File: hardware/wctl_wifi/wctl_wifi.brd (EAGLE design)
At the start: 40.4 x 26.8 mm, 9 parts, among them U1 Value

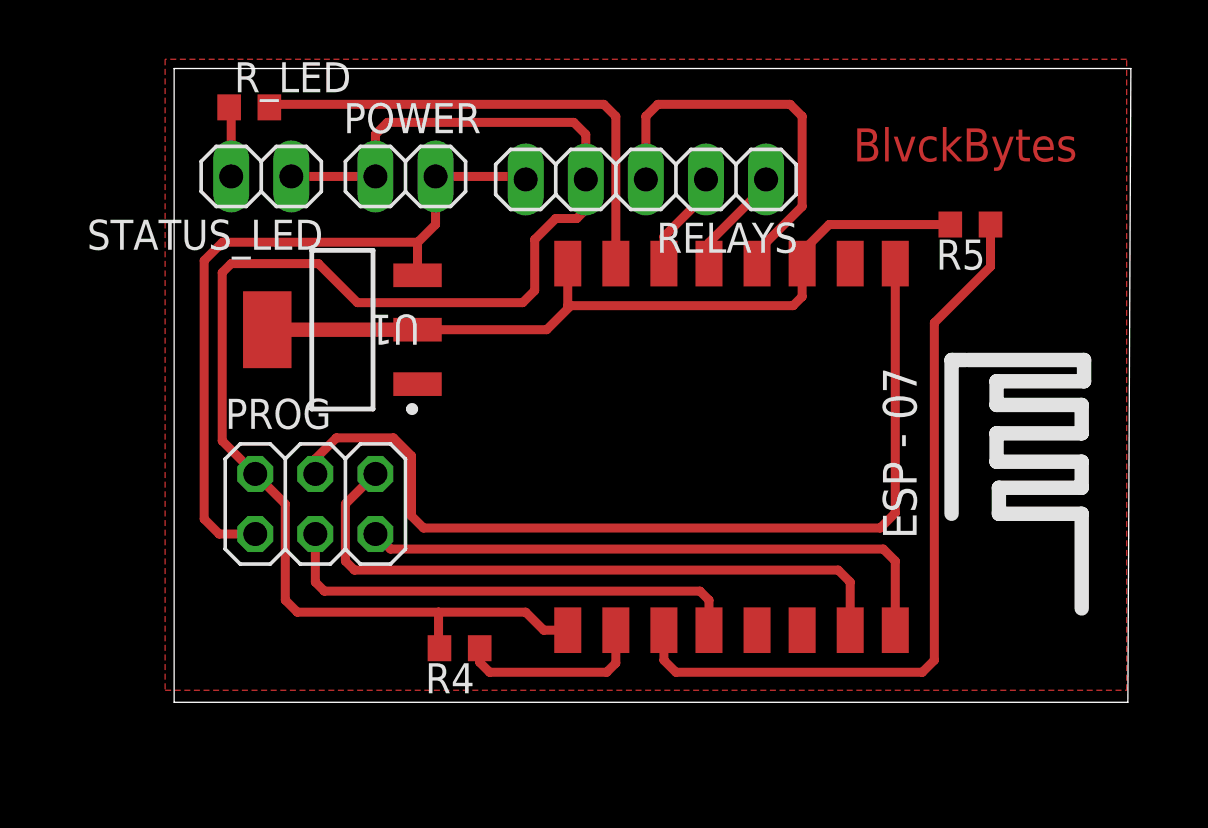
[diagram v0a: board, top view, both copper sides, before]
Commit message: Migrated back to ESP32, updated pins in code and updated hardware, also updated readme
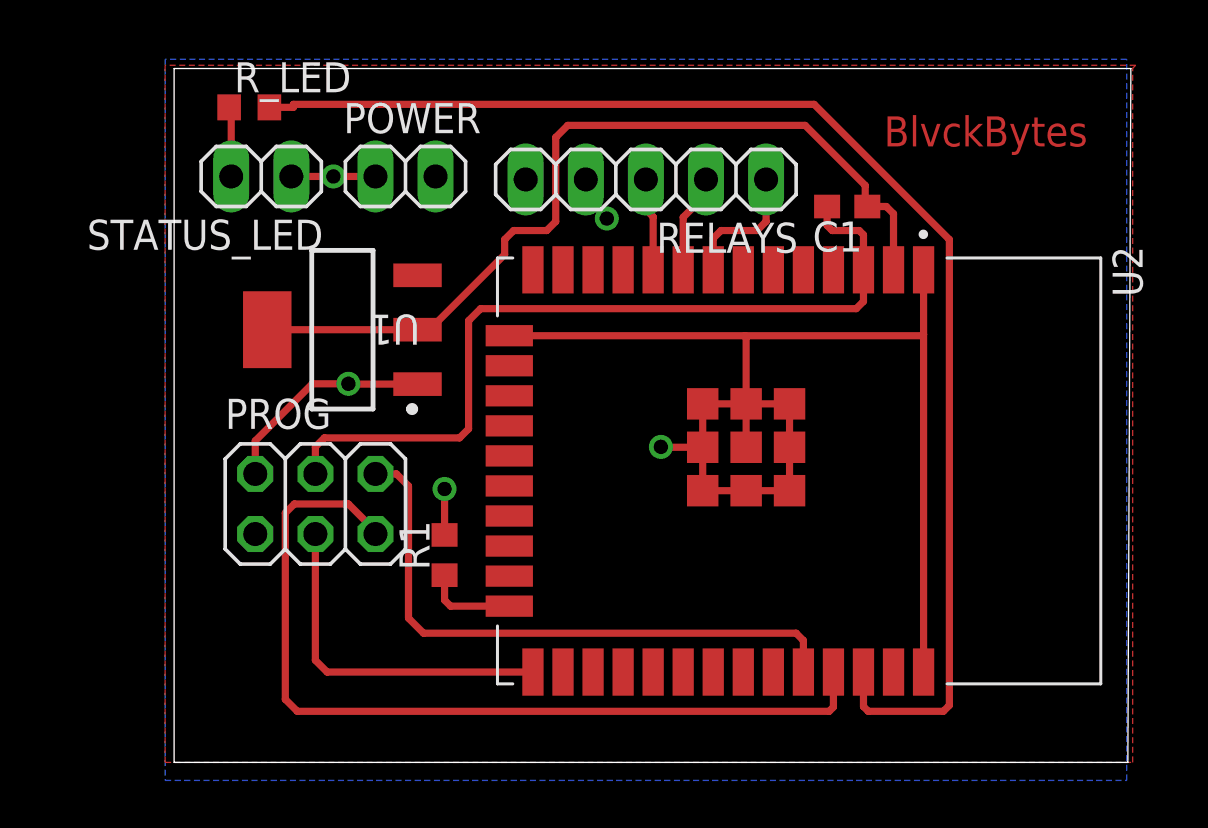
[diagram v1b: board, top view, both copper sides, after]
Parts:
- removed R4, R5: 10k, rcl:R0603
- removed U$2: ESP07, esp-07:ESP07
- added C1: (no value), rcl:C0603
- added R1: 10k, rcl:R0603
- added U2: ESP32-WROOM-32D, ESP32-WROOM-32D:MODULE_ESP32-WROOM-32D
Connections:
- removed net N$4: R_LED.2, U$2.GPIO13
- removed net N$6: R5.1, U$2.GPIO2
- removed net N$7: R4.1, U$2.GPIO15
- new net N$2: R_LED.2, U2.36
- new net N$3: R1.1, U2.24
- net +3V3: now also C1.1, U2.2; no longer R5.2, U$2.CH_PD, U$2.VCC
- net GND: now also R1.2, U2.1, U2.15, U2.38, U2.39_1, U2.39_2, U2.39_3, U2.39_4, U2.39_5, U2.39_6, U2.39_7, U2.39_8, U2.39_9; no longer R4.2, U$2.GND
- net PROG: now also U2.25; no longer U$2.GPIO0
- net RELAYS_DATA: now also U2.10; no longer U$2.GPIO16
- net RELAYS_SHIFT: now also U2.8; no longer U$2.GPIO14
- net RELAYS_STORE: now also U2.9; no longer U$2.GPIO12
- net RESET: now also C1.2, U2.3; no longer U$2.RESET
- net RX: now also U2.34; no longer U$2.RX
- net TX: now also U2.35; no longer U$2.TX
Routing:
- net N$2: track 0.00 -> 56.2 mm
- net N$6: track 32.5 -> 0.00 mm
- net +5V: track 31.1 -> 0.00 mm
- net N$4: track 21.3 -> 0.00 mm
- net RELAYS_DATA: track 16.7 -> 3.95 mm
- net TX: track 25.4 -> 37.6 mm
- net N$7: track 8.08 -> 0.00 mm
- net GND: track 65.9 -> 72.8 mm, vias 0 -> 5
- net PROG: track 20.3 -> 14.7 mm
- net RESET: track 39.4 -> 34.9 mm
- net N$3: track 0.00 -> 3.90 mm
- net +3V3: track 33.7 -> 36.9 mm
- net RX: track 27.9 -> 25.6 mm
- net RELAYS_SHIFT: track 4.56 -> 5.64 mm
- added copper zone on layer 1, net +5V
- added copper zone on layer 16, net GND
- removed copper zone on layer 1, net GND
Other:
- board size 40.4 x 26.8 mm -> 40.4 x 29.3 mm

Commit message: hardware: updated wifi board
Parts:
- added R2: 10k, rcl:R0603
- added U$1: SD_SLOT, sd_slot:SD_SLOT
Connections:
- new net CS: U$1.2, U2.29
- new net MISO: U$1.7, U2.31
- new net MOSI: U$1.3, U2.37
- new net SCK: U$1.5, U2.30
- new net ~SWITCH: R2.2, U$1.9, U2.26
- net +3V3: now also R2.1, U$1.4
- net GND: now also U$1.6, U$1.SH1, U$1.SH2, U$1.SH3, U$1.SH4
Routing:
- net ~SWITCH: track 0.00 -> 26.9 mm, vias 0 -> 1
- net MISO: track 0.00 -> 18.2 mm, vias 0 -> 1
- net +3V3: track 36.9 -> 54.5 mm, vias 0 -> 1
- net CS: track 0.00 -> 14.2 mm, vias 0 -> 1
- net SCK: track 0.00 -> 12.3 mm, vias 0 -> 1
- net MOSI: track 0.00 -> 11.3 mm, vias 0 -> 1
- net RX: track 25.6 -> 34.2 mm
- net GND: track 72.8 -> 73.2 mm, vias 5 -> 6
